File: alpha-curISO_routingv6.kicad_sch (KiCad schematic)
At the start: 28 parts, among them J2 SWD, U1 RP2040, U5 74AHCT1G125

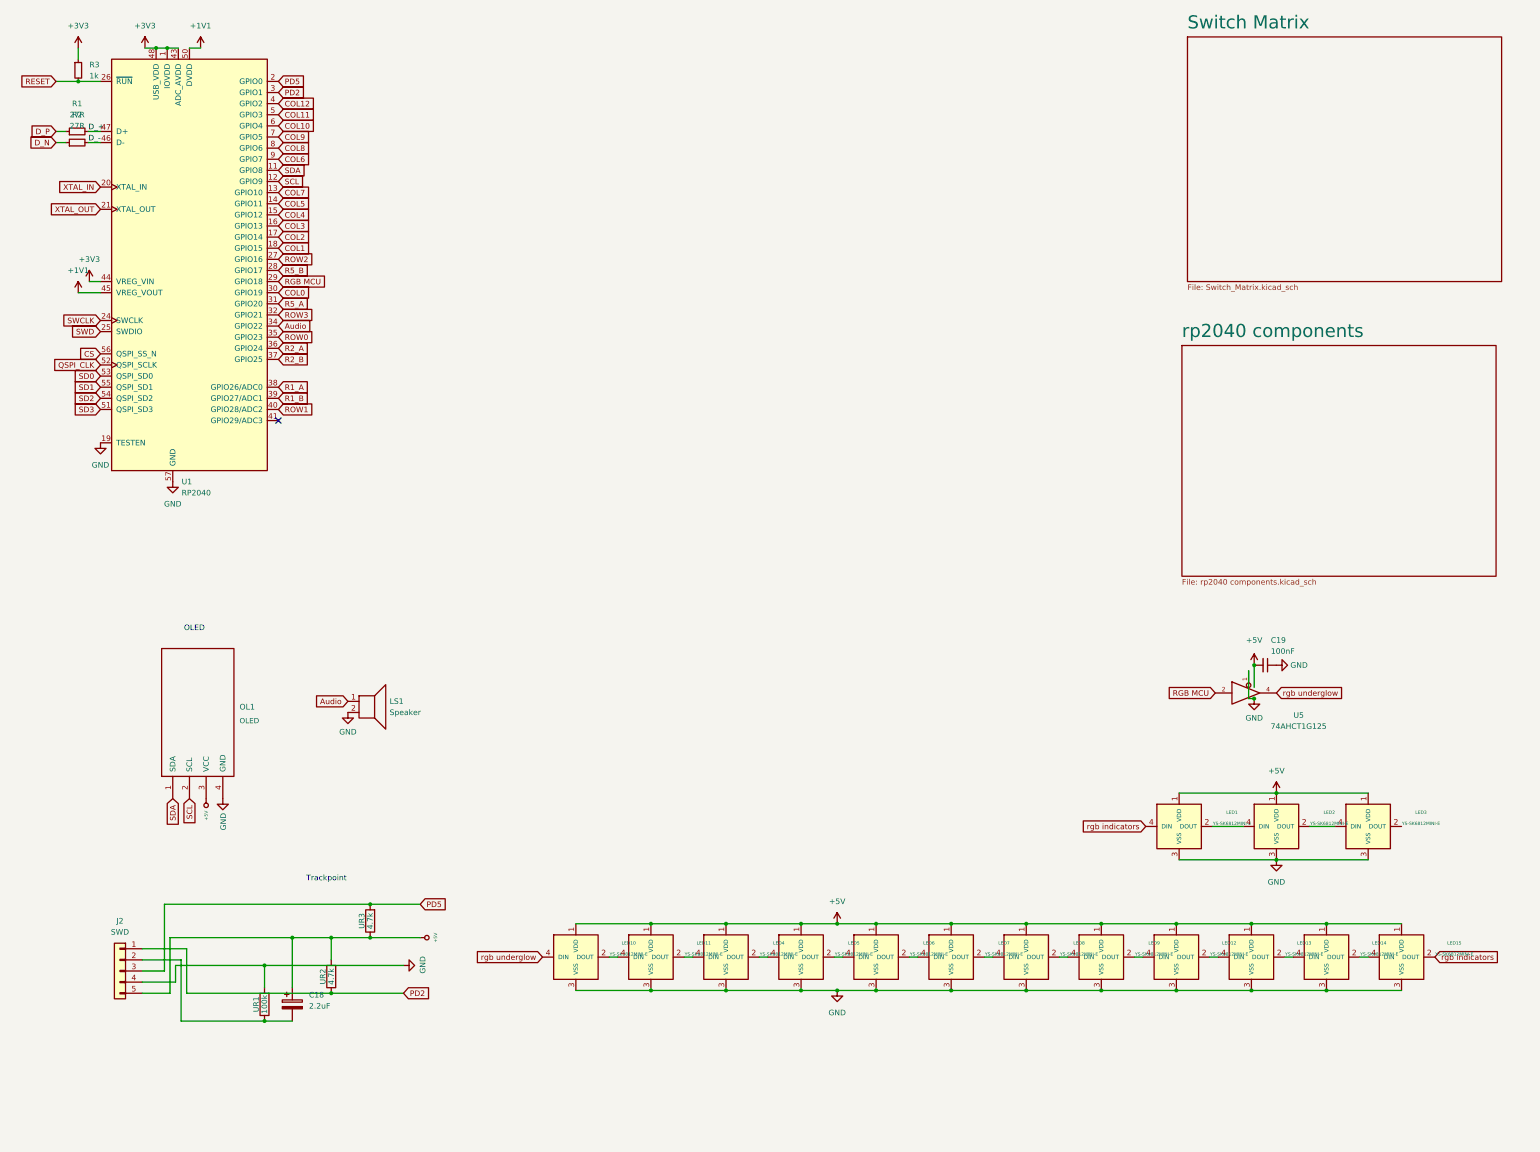
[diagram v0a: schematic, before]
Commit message: added capacitors for each led, some routing tweaks
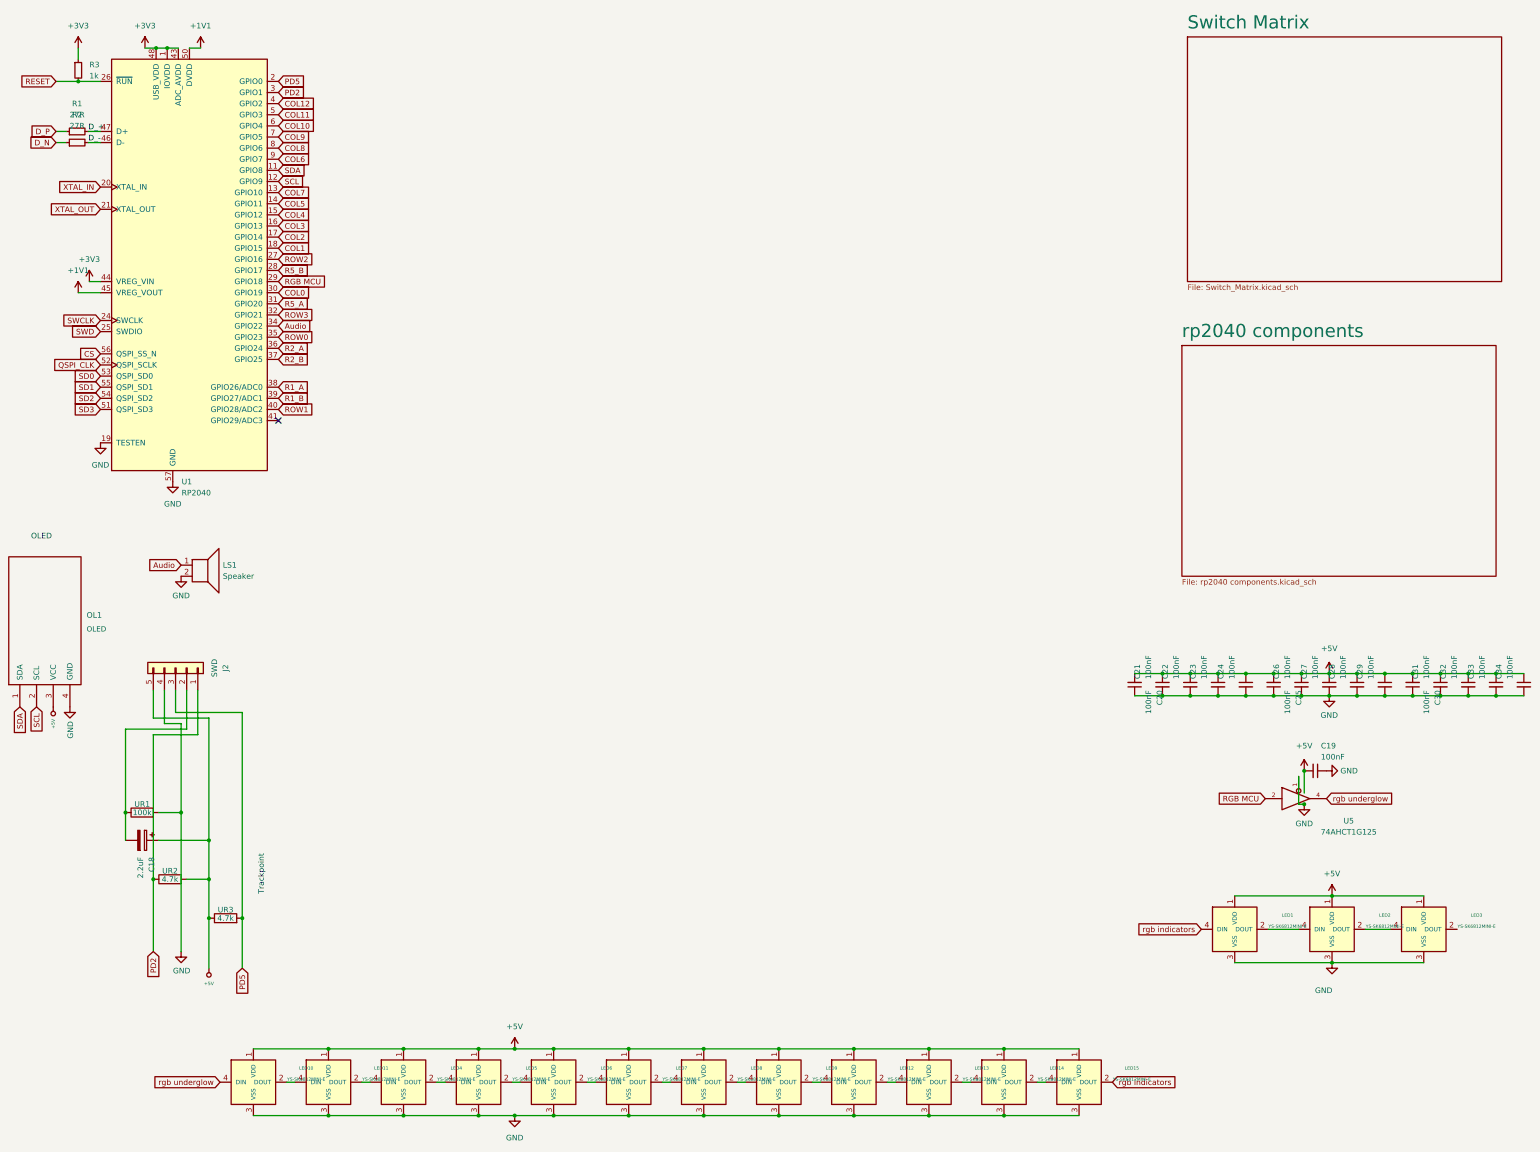
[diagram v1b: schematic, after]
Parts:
- added C20, C21, C22, C23, C24, C25, C26, C27, C28, C29, C30, C31, C32, C33, C34: 100nF, Capacitor_SMD:C_0402_1005Metric, symbol Device:C_Small
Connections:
- net +5V: now also C20.2, C21.1, C22.1, C23.1, C24.1, C25.2, C26.1, C27.1, C28.1, C29.1, C30.2, C31.1, C32.1, C33.1, C34.1
- net GND: now also C20.1, C21.2, C22.2, C23.2, C24.2, C25.1, C26.2, C27.2, C28.2, C29.2, C30.1, C31.2, C32.2, C33.2, C34.2
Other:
- moved on the sheet: C18, C19, J2, LED1, LED10, LED11, LED12, LED13, LED14, LED15, LED2, LED3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

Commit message: oled changed to 3v3
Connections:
- net +3V3: now also OL1.3 (VCC)
- net +5V: no longer OL1.3 (VCC)
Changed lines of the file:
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@@
+    (pin "1")
+  )
+  (symbol (lib_name "+3V3_1") (lib_id "power:+3V3") (at 28.575 179.705 180) (unit 1)
+    (in_bom yes) (on_board yes) (fields_autoplaced)
+    (property "Reference" "#PWR?" (id 0) (at 28.575 175.895 0)
+      (effects (font (size 1.27 1.27)) hide)
+    )
+    (property "Value" "+3V3" (id 1) (at 28.575 184.15 0))
+    (property "Footprint" "" (id 2) (at 28.575 179.705 0)
+      (effects (font (size 1.27 1.27)) hide)
+    )
+    (property "Datasheet" "" (id 3) (at 28.575 179.705 0)
+      (effects (font (size 1.27 1.27)) hide)
+    )
     (pin "1")
   )
@@
     (pin "2")
   )
-  (symbol (lib_id "keyboard_parts:+5V") (at 28.575 179.705 180) (unit 1)
-    (in_bom yes) (on_board yes)
-    (property "Reference" "#PWR0137" (id 0) (at 28.575 178.943 0)
-      (effects (font (size 0.508 0.508)) hide)
-    )
-    (property "Value" "+5V" (id 1) (at 28.575 182.4482 90)
-      (effects (font (size 0.762 0.762)) (justify left))
-    )
-    (property "Footprint" "" (id 2) (at 28.575 179.705 0)
-      (effects (font (size 1.524 1.524)))
-    )
-    (property "Datasheet" "" (id 3) (at 28.575 179.705 0)
-      (effects (font (size 1.524 1.524)))
-    )
-    (pin "1")
-  )
   (symbol (lib_id "Device:C_Small") (at 351.79 174.625 0) (unit 1)
     (in_bom yes) (on_board yes)
@@
       (reference "#PWR0136") (unit 1) (value "GND") (footprint "")
     )
-    (path "/a7a73d9b-4fdb-44fe-86ac-6bf41412f058"
-      (reference "#PWR0137") (unit 1) (value "+5V") (footprint "")
-    )
     (path "/1d1a01f8-a74a-4ce9-acc5-911524b414cb"
       (reference "#PWR0138") (unit 1) (value "GND") (footprint "")
@@
       (reference "#PWR0155") (unit 1) (value "GND") (footprint "")
     )
+    (path "/1670c66e-bb68-4c8a-b466-ad045f3b87cd"
+      (reference "#PWR?") (unit 1) (value "+3V3") (footprint "")
+    )
     (path "/ed815977-8ce9-43bf-9f7d-c601496617ea/cce79384-81e6-4921-84d5-1511ce8fbc31"

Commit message: trackpoint changed to 3v3
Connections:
- net +3V3: now also C18.1, J2.5 (Pin_5), UR2.2, UR3.1
- net +5V: no longer C18.1, J2.5 (Pin_5), UR2.2, UR3.1
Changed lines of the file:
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@@
     (pin "2")
+  )
+  (symbol (lib_name "+3V3_1") (lib_id "power:+3V3") (at 64.135 239.395 180) (unit 1)
+    (in_bom yes) (on_board yes) (fields_autoplaced)
+    (property "Reference" "#PWR?" (id 0) (at 64.135 235.585 0)
+      (effects (font (size 1.27 1.27)) hide)
+    )
+    (property "Value" "+3V3" (id 1) (at 64.135 243.84 0))
+    (property "Footprint" "" (id 2) (at 64.135 239.395 0)
+      (effects (font (size 1.27 1.27)) hide)
+    )
+    (property "Datasheet" "" (id 3) (at 64.135 239.395 0)
+      (effects (font (size 1.27 1.27)) hide)
+    )
+    (pin "1")
   )
   (symbol (lib_id "Device:C_Small") (at 364.49 174.625 0) (unit 1)
@@
     (property "Datasheet" "" (id 3) (at 62.23 29.21 0)
       (effects (font (size 1.27 1.27)) hide)
-    )
-    (pin "1")
-  )
-  (symbol (lib_id "keyboard_parts:+5V") (at 64.135 239.395 180) (unit 1)
-    (in_bom yes) (on_board yes)
-    (property "Reference" "#PWR0139" (id 0) (at 64.135 238.633 0)
-      (effects (font (size 0.508 0.508)) hide)
-    )
-    (property "Value" "+5V" (id 1) (at 64.135 242.9002 0)
-      (effects (font (size 0.762 0.762)))
-    )
-    (property "Footprint" "" (id 2) (at 64.135 239.395 0)
-      (effects (font (size 1.524 1.524)))
-    )
-    (property "Datasheet" "" (id 3) (at 64.135 239.395 0)
-      (effects (font (size 1.524 1.524)))
     )
     (pin "1")
@@
       (reference "#PWR0138") (unit 1) (value "GND") (footprint "")
     )
-    (path "/5d13b254-319a-424b-93ff-fb25d71472df"
-      (reference "#PWR0139") (unit 1) (value "+5V") (footprint "")
-    )
     (path "/25241a54-1300-411c-bb0d-b8e1b4e25576"
       (reference "#PWR0140") (unit 1) (value "GND") (footprint "")
@@
       (reference "#PWR0155") (unit 1) (value "GND") (footprint "")
     )
+    (path "/0496c3f1-f9e9-4ce3-8cee-cd8468c66ede"
+      (reference "#PWR?") (unit 1) (value "+3V3") (footprint "")
+    )
     (path "/1670c66e-bb68-4c8a-b466-ad045f3b87cd"
